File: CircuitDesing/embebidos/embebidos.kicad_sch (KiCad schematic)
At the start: 0 parts

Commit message: Avance esquemático
Subcircuitos
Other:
- added sheet Actuadores (Actuadores.kicad_sch)
- added sheet Potencia (Potencia.kicad_sch)
- added sheet Sensores (Sensores.kicad_sch)

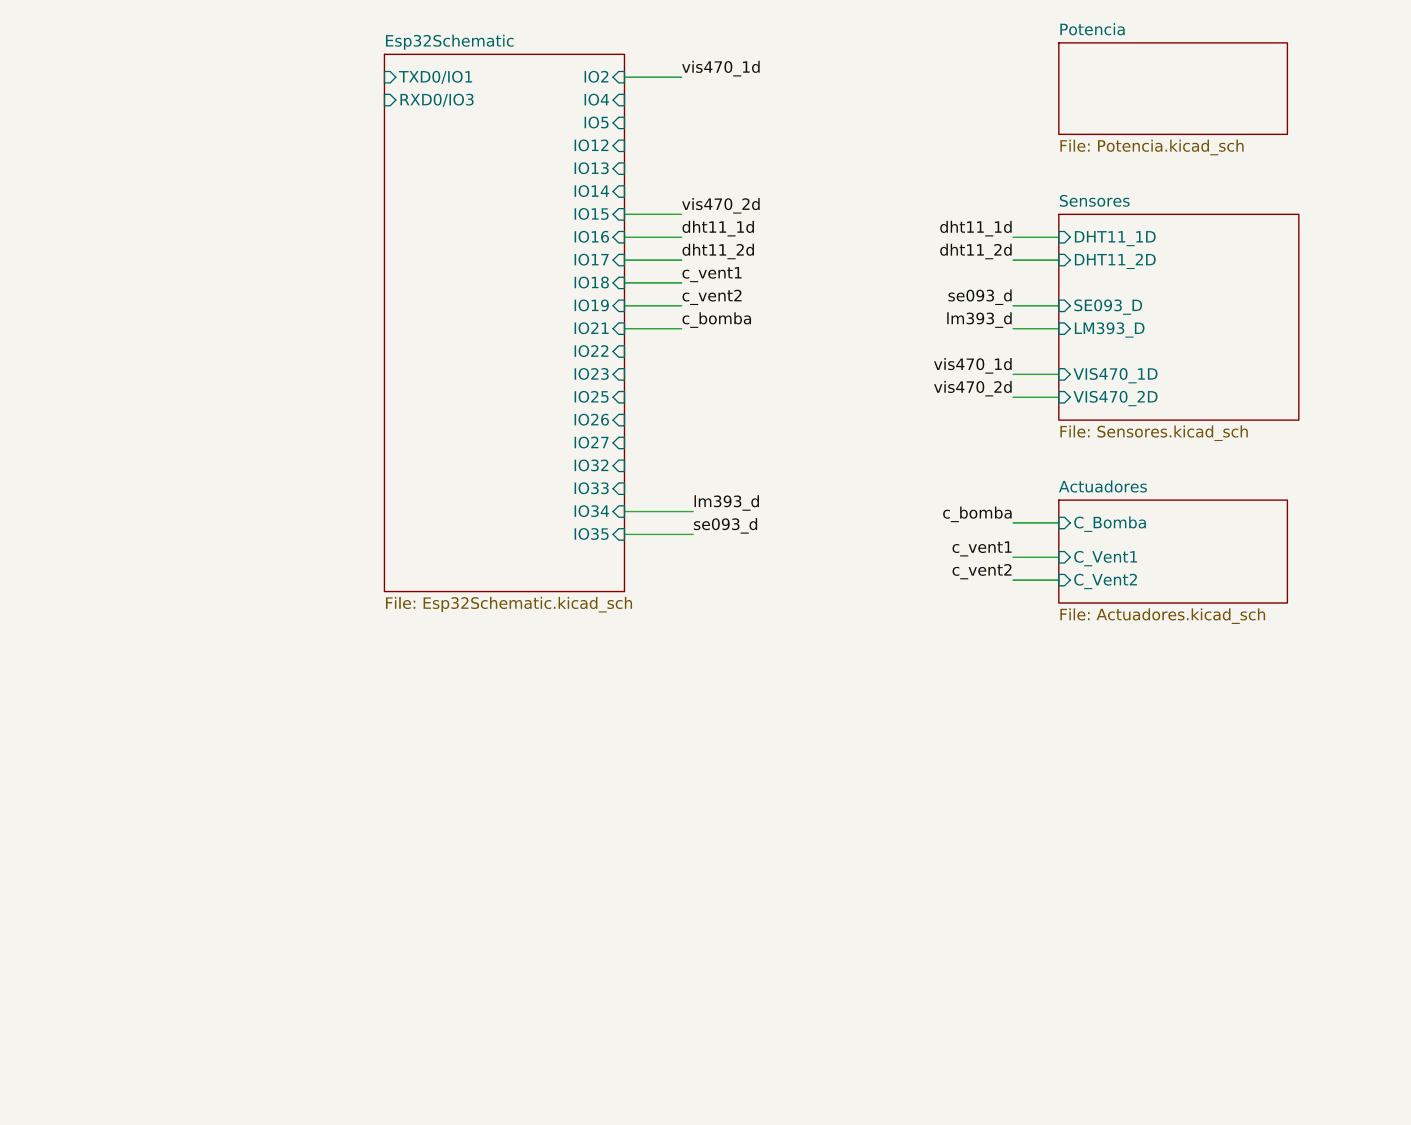
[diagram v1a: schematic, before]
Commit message: Potencia
Primera propuesta del esquema de potencia
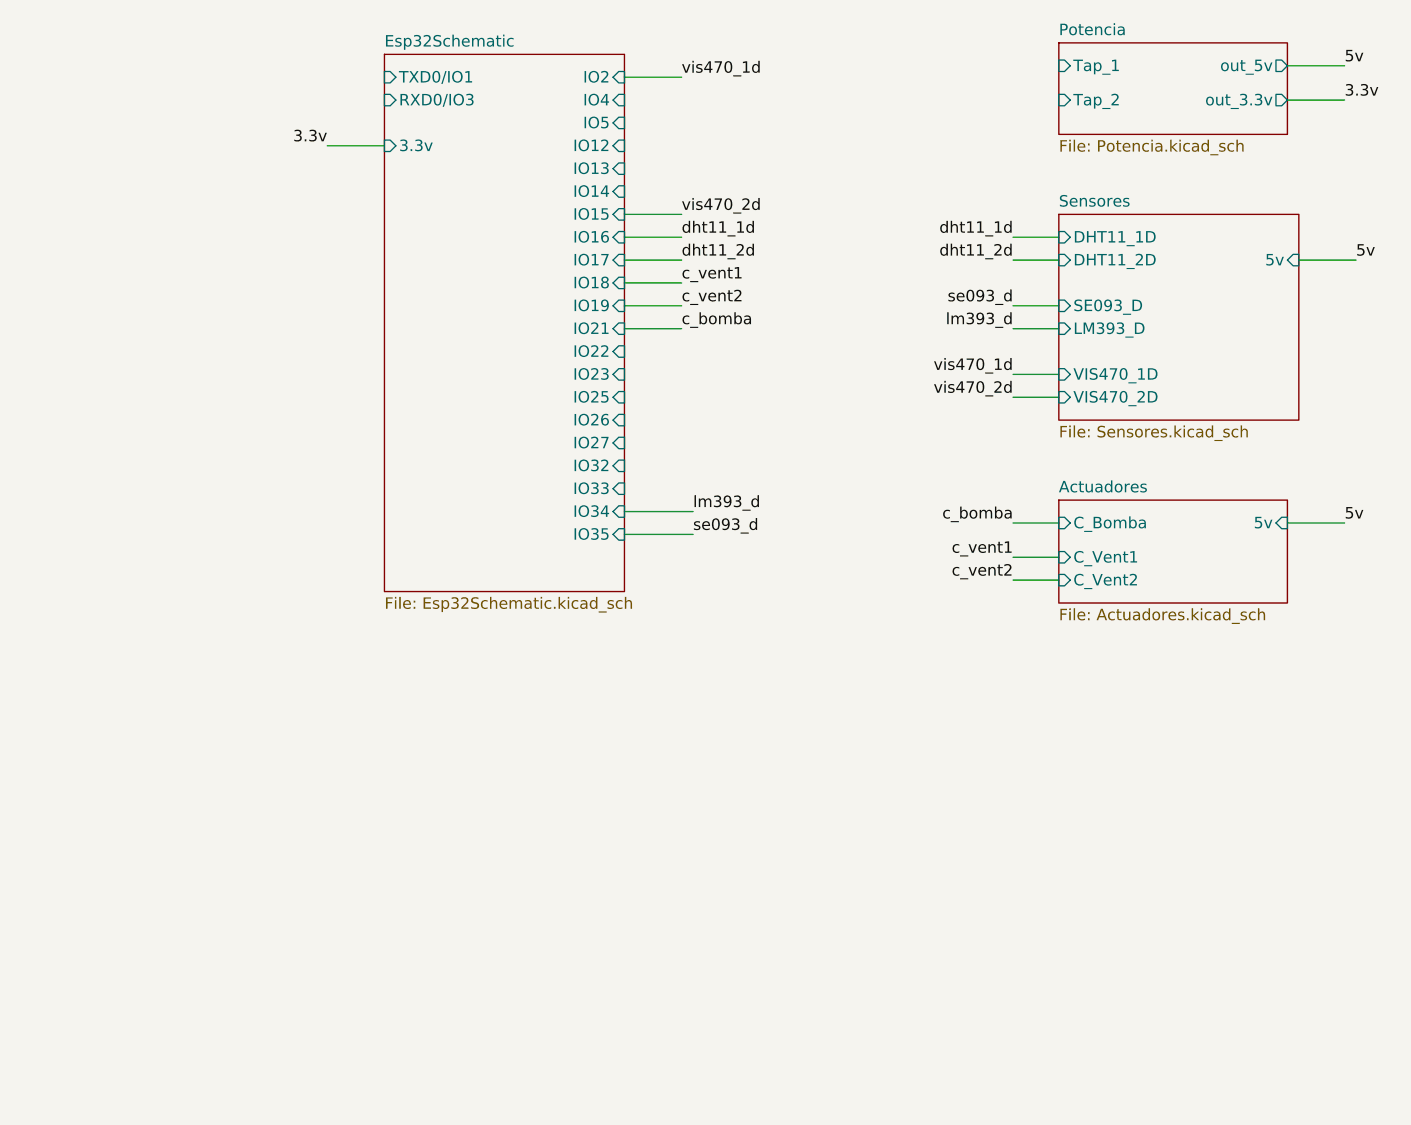
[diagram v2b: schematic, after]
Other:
- sheet Actuadores ports: added 5v; removed none
- sheet Esp32Schematic ports: added 3.3v; removed none
- sheet Potencia ports: added Tap_1, Tap_2, out_3.3v, out_5v; removed none
- sheet Sensores ports: added 5v; removed none

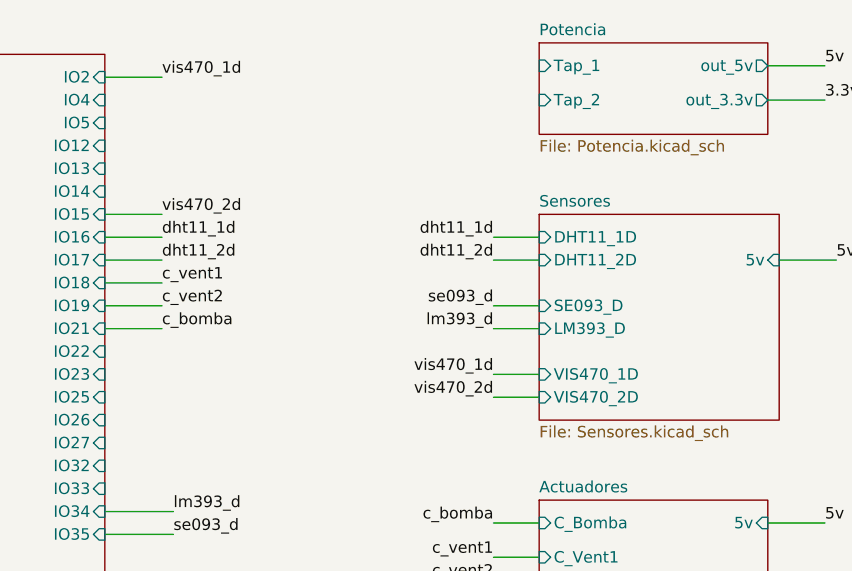
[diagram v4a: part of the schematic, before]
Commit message: Sensor Ultrasonido
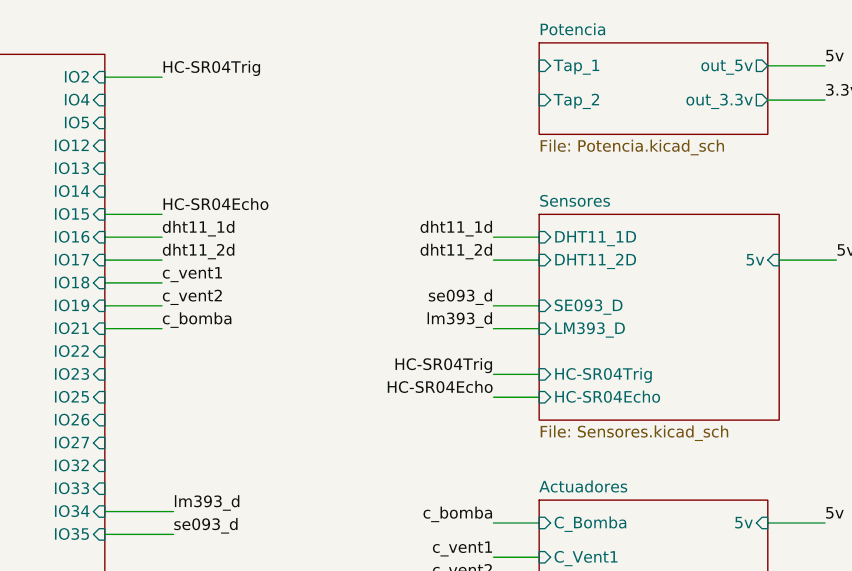
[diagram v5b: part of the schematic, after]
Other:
- sheet Sensores ports: added HC-SR04Echo, HC-SR04Trig; removed VIS470_1D, VIS470_2D
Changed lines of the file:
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@@
-    (effects (font (size 1.27 1.27)) (justify left bottom))
-  )
-  (label "vis470_1d" (at 125.73 63.5 0)
     (effects (font (size 1.27 1.27)) (justify left bottom))
   )
@@
     (effects (font (size 1.27 1.27)) (justify left bottom))
   )
-  (label "vis470_1d" (at 162.56 96.52 180)
-    (effects (font (size 1.27 1.27)) (justify right bottom))
-  )
-  (label "vis470_2d" (at 125.73 78.74 0)
-    (effects (font (size 1.27 1.27)) (justify left bottom))
+  (label "HC-SR04Trig" (at 162.56 96.52 180)
+    (effects (font (size 1.27 1.27)) (justify right bottom))
   )
   (label "c_bomba" (at 162.56 113.03 180)
@@
     (effects (font (size 1.27 1.27)) (justify right bottom))
   )
+  (label "HC-SR04Echo" (at 125.73 78.74 0)
+    (effects (font (size 1.27 1.27)) (justify left bottom))
+  )
   (label "dht11_2d" (at 162.56 83.82 180)
     (effects (font (size 1.27 1.27)) (justify right bottom))
@@
     (effects (font (size 1.27 1.27)) (justify left bottom))
   )
+  (label "HC-SR04Trig" (at 125.73 63.5 0)
+    (effects (font (size 1.27 1.27)) (justify left bottom))
+  )
   (label "dht11_1d" (at 125.73 81.28 0)
     (effects (font (size 1.27 1.27)) (justify left bottom))
   )
-  (label "vis470_2d" (at 162.56 99.06 180)
+  (label "HC-SR04Echo" (at 162.56 99.06 180)
     (effects (font (size 1.27 1.27)) (justify right bottom))
   )
@@
       (effects (font (size 1.27 1.27)) (justify left))
     )
-    (pin "VIS470_2D" input (at 167.64 99.06 180)
-      (effects (font (size 1.27 1.27)) (justify left))
-    )
-    (pin "VIS470_1D" input (at 167.64 96.52 180)
-      (effects (font (size 1.27 1.27)) (justify left))
-    )
     (pin "5v" input (at 194.31 83.82 0)
       (effects (font (size 1.27 1.27)) (justify right))
+    )
+    (pin "HC-SR04Trig" input (at 167.64 96.52 180)
+      (effects (font (size 1.27 1.27)) (justify left))
+    )
+    (pin "HC-SR04Echo" input (at 167.64 99.06 180)
+      (effects (font (size 1.27 1.27)) (justify left))
     )
   )
@@
       (reference "#PWR?") (unit 1) (value "GND") (footprint "")
     )
-    (path "/4a4a8db1-1786-4804-b37e-204adf7255cc/6211d82a-0d41-443e-9d2a-69794e79f779"
-      (reference "#PWR?") (unit 1) (value "GND") (footprint "")
-    )
     (path "/4a4a8db1-1786-4804-b37e-204adf7255cc/6a843c8e-b0e6-477e-abf7-d31b7366eead"
       (reference "#PWR?") (unit 1) (value "GND") (footprint "")
@@
       (reference "DHT11_2") (unit 1) (value "Conn_01x03") (footprint "")
     )
+    (path "/4a4a8db1-1786-4804-b37e-204adf7255cc/0823b20b-a4db-47c0-9c4c-50c512401f1f"
+      (reference "J?") (unit 1) (value "Conn_01x04") (footprint "")
+    )
     (path "/4a4a8db1-1786-4804-b37e-204adf7255cc/49f3433d-4d41-4994-b007-3fd9fa4c7900/4574ea61-9318-4696-912e-66107addb1a9"
       (reference "J?") (unit 1) (value "Conn_01x02") (footprint "")
@@
       (reference "U?") (unit 1) (value "LM1117-3.3") (footprint "")
     )
-    (path "/4a4a8db1-1786-4804-b37e-204adf7255cc/9af86cef-568c-4b37-8b0d-af2a5e982b7e"
-      (reference "VIS470") (unit 1) (value "Conn_01x03") (footprint "")
-    )
-    (path "/4a4a8db1-1786-4804-b37e-204adf7255cc/829e8a88-dee8-4c29-92a3-2b09628c8bc3"
-      (reference "VIS?") (unit 1) (value "Conn_01x03") (footprint "")
-    )
     (path "/baefe8d2-116f-4132-b22d-e866645ad738/52325a88-4095-45a0-b602-a8ec1792f959"
